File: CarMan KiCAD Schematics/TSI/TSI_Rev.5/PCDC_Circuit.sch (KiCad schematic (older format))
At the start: 55 parts, among them IC4 TS431ILT, K1 APAN3105, Q1 ZVP1320F, Q5 SI1302DL-T1-E3, U12 REF3033, U19 74HC00, U20 MC7805BDTRKG, U21 MCP6004, U29 SN74LVC1G08DCKR, U31 TLP293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

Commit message: Bug Fixins
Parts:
- removed C1: 0.47u, Capacitor_SMD:C_0805_2012Metric_Pad1.15x1.40mm_HandSolder, symbol pspice:CAP
- removed L1: 2.2uH, Inductor_SMD:L_0805_2012Metric_Pad1.15x1.40mm_HandSolder, symbol pspice:INDUCTOR
- removed PS1: THN_30-2415WI, symbol TSI_Rev.5-rescue:THN_30-2415WI-CarMan_KiCAD_Library-TSI_Rev.5-rescue
- removed U12: REF3033, Package_TO_SOT_SMD:SOT-23, symbol Reference_Voltage:REF3033
- added PS1: THN_30-2415WI, symbol CarMan_KiCAD_Library:THN_30-2415WI
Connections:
- net 24V: now also PS1.1 (+VIN(VCC))
- net AIRS-: now also PS1.2 (-VIN(GND))
- net DC_RELAY-: now also PS1.5 (-VOUT)
- net PC_RELAY+: now also PS1.3 (+VOUT)
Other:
- note removed: "3.3V Voltage Reference"
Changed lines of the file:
@@
 Connection ~ 13050 3850
-Wire Wire Line
-	14650 3050 14300 3050
 Wire Wire Line
 	14300 3050 14300 3150
@@
 Wire Wire Line
 	6500 7750 6250 7750
-$Comp
-L Reference_Voltage:REF3033 U12
-U 1 1 5FAD159D
-P 12550 9050
-F 0 "U12" H 12321 9096 50  0000 R CNN
-F 1 "REF3033" H 12321 9005 50  0000 R CIN
-F 2 "Package_TO_SOT_SMD:SOT-23" H 12550 8600 50  0001 C CIN
-F 3 "http://www.ti.com/lit/ds/symlink/ref3033.pdf" H 12650 8700 50  0001 C CIN
-	1    12550 9050
-	1    0    0    -1
-$EndComp
 Wire Notes Line
 	11400 9900 16000 9900
@@
 Wire Notes Line
 	11400 6350 11400 9900
-$Comp
-L pspice:CAP C1
-U 1 1 5FAE51C2
-P 11600 9050
-F 0 "C1" H 11650 9150 50  0000 L CNN
-F 1 "0.47u" H 11650 8950 50  0000 L CNN
-F 2 "Capacitor_SMD:C_0805_2012Metric_Pad1.15x1.40mm_HandSolder" H 11600 9050 50  0001 C CNN
-F 3 "~" H 11600 9050 50  0001 C CNN
-	1    11600 9050
-	1    0    0    -1
-$EndComp
-Wire Wire Line
-	11600 9400 12450 9400
-Wire Wire Line
-	12450 9400 12450 9350
-Wire Wire Line
-	11600 8700 11600 8800
-Wire Wire Line
-	11600 8700 12450 8700
-Wire Wire Line
-	12450 8700 12450 8750
-Wire Wire Line
-	11600 9400 11600 9300
-Wire Wire Line
-	13050 9050 12850 9050
-Text Label 12450 8600 0    79   ~ 0
-5HV
-Text Label 12450 9450 0    79   ~ 0
-IO_Ground
-Text Label 13050 9050 0    79   ~ 0
-3.3_VREF
-Wire Wire Line
-	12450 9400 12450 9450
-Connection ~ 12450 9400
-Wire Wire Line
-	12450 8600 12450 8700
-Connection ~ 12450 8700
-Text Notes 11550 9750 0    79   ~ 0
-3.3V Voltage Reference
 Wire Wire Line
 	4900 10600 5100 10600
@@
 Wire Wire Line
 	3850 9650 4150 9650
-$Comp
-L TSI_Rev.5-rescue:THN_30-2415WI-CarMan_KiCAD_Library-TSI_Rev.5-rescue PS1
-U 1 1 5FBB1814
-P 5750 9650
-F 0 "PS1" H 5725 10081 79  0000 C CNN
-F 1 "THN_30-2415WI" H 5725 9946 79  0000 C CNN
-F 2 "" H 5500 9700 79  0001 C CNN
-F 3 "https://www.snapeda.com/parts/THN%2030-2415WI/Traco%20Power/datasheet/" H 5500 9700 79  0001 C CNN
-	1    5750 9650
-	1    0    0    -1
-$EndComp
 Wire Wire Line
 	6700 9650 6450 9650
@@
 Connection ~ 4150 9100
 Wire Wire Line
-	4150 9100 4250 9100
-Wire Wire Line
 	4900 9500 4950 9500
 Wire Wire Line
@@
 Text Label 6700 9800 2    47   ~ 0
 24HV
-Wire Wire Line
-	4750 9100 4900 9100
-$Comp
-L pspice:INDUCTOR L1
-U 1 1 61234915
-P 4500 9100
-F 0 "L1" H 4500 9315 50  0000 C CNN
-F 1 "2.2uH" H 4500 9224 50  0000 C CNN
-F 2 "Inductor_SMD:L_0805_2012Metric_Pad1.15x1.40mm_HandSolder" H 4500 9100 50  0001 C CNN
-F 3 "~" H 4500 9100 50  0001 C CNN
-	1    4500 9100
-	1    0    0    -1
-$EndComp
 Wire Wire Line
 	4900 9100 4900 9500
@@
 Text Notes 7200 2500 0    59   ~ 0
 NAND Package \nPower Supplies
+$Comp
+L power:PWR_FLAG #FLG0107
+U 1 1 60081B98
+P 14350 7750
+F 0 "#FLG0107" H 14350 7825 50  0001 C CNN
+F 1 "PWR_FLAG" V 14350 7878 50  0000 L CNN
+F 2 "" H 14350 7750 50  0001 C CNN
+F 3 "~" H 14350 7750 50  0001 C CNN
+	1    14350 7750
+	0    1    1    0
+$EndComp
+Wire Wire Line
+	4150 9100 4900 9100
+$Comp
+L CarMan_KiCAD_Library:THN_30-2415WI PS1
+U 1 1 601034A0
+P 5750 9650
+F 0 "PS1" H 5700 10131 79  0000 C CNN
+F 1 "THN_30-2415WI" H 5700 9996 79  0000 C CNN
+F 2 "" H 5450 9750 79  0001 C CNN
+F 3 "" H 5450 9750 79  0001 C CNN
+	1    5750 9650
+	1    0    0    -1
+$EndComp
+Wire Wire Line
+	14300 3050 14650 3050
 $EndSCHEMATC

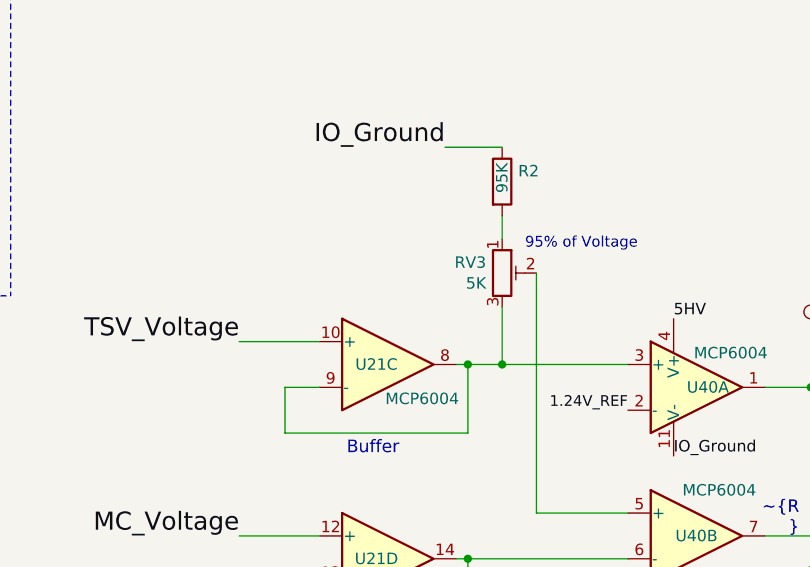
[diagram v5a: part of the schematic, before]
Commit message: TSI Footprinting (~95%) - Added Silk Screen Images from last years projects (not added to any libraries, just folder)
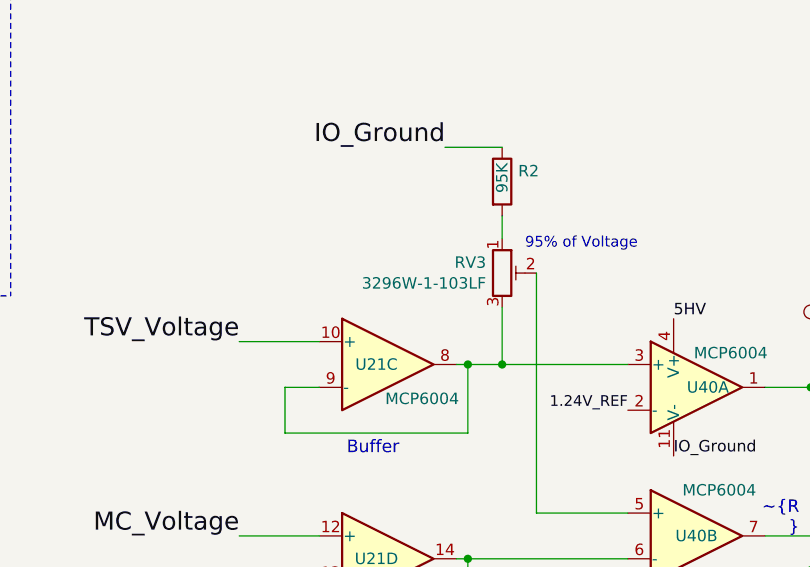
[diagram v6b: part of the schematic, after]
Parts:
- RV3: value 5K -> 3296W-1-103LF; footprint (none) -> Potentiometer_THT:Potentiometer_Bourns_3296W_Vertical
- RV5: footprint (none) -> TSI_Rev_2021_Footprint_Lib:23BR10KLFTR
- U9: footprint (none) -> TSI_Rev_2021_Footprint_Lib:SOT230P700X180-4N-speical
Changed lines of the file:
@@
 P 4500 2350
 F 0 "RV3" H 4430 2396 50  0000 R CNN
-F 1 "5K" H 4430 2305 50  0000 R CNN
-F 2 "" H 4500 2350 50  0001 C CNN
+F 1 "3296W-1-103LF" H 4430 2305 50  0000 R CNN
+F 2 "Potentiometer_THT:Potentiometer_Bourns_3296W_Vertical" H 4500 2350 50  0001 C CNN
 F 3 "~" H 4500 2350 50  0001 C CNN
 	1    4500 2350
@@
 F 0 "RV5" H 14280 7104 50  0000 R CNN
 F 1 "R_POT_TRIM" H 14280 7195 50  0000 R CNN
-F 2 "" H 14350 7150 50  0001 C CNN
+F 2 "TSI_Rev_2021_Footprint_Lib:23BR10KLFTR" H 14350 7150 50  0001 C CNN
 F 3 "~" H 14350 7150 50  0001 C CNN
 	1    14350 7150
@@
 F 0 "U9" H 10000 2950 55  0000 L CNN
 F 1 "STN3NF06L" H 9800 2850 55  0000 L CNN
-F 2 "" H 9850 3400 55  0001 C CNN
+F 2 "TSI_Rev_2021_Footprint_Lib:SOT230P700X180-4N-speical" H 9850 3400 55  0001 C CNN
 F 3 "" H 9850 3400 55  0001 C CNN
 	1    10250 3050

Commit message: TSI Footprinting (~98%) - Assigned U41 footprint to PS1 footprint. Not able to find PS1 footprint. Referenced last years design and took measurement on PCB. Measured as the same distances between points - Need footprints for K2, K3, K4 & J1
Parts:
- PS1: footprint (none) -> TSI_Rev_2021_Footprint_Lib:CONV_PDQ10-Q24-D5-D
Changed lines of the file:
@@
 F 0 "PS1" H 5700 10131 79  0000 C CNN
 F 1 "THN_30-2415WI" H 5700 9996 79  0000 C CNN
-F 2 "" H 5450 9750 79  0001 C CNN
+F 2 "TSI_Rev_2021_Footprint_Lib:CONV_PDQ10-Q24-D5-D" H 5450 9750 79  0001 C CNN
 F 3 "" H 5450 9750 79  0001 C CNN
 	1    5750 9650

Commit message: Started TSI PCB
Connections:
- net MC+ renamed MC_Voltage
- net TSV_V renamed TSV_Voltage
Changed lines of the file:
@@
 Throttle_HV
 Text HLabel 1300 1050 0    50   Input ~ 0
-MC+
+MC_Voltage
 Text HLabel 1300 950  0    50   Input ~ 0
 HV-
@@
 95% of Voltage
 Text HLabel 1300 1150 0    50   Input ~ 0
-TSV_V
+TSV_Voltage
 Text HLabel 1300 1250 0    50   Input ~ 0
 IO_Ground
